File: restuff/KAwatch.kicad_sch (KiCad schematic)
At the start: 24 parts, among them J1 Conn_01x08, J2 USB_C_Receptacle_PowerOnly_6P, J3 Conn_01x02, J4 Conn_01x02, Q1 Q_NPN_BCE, SW1 SW_Push, U1 ESP32-WROOM-32E, U2 MCP73831-2-OT, U3 AMS1117-3.3

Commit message: footprint assignment complete
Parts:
- C1, C2, C3, C4, C5: footprint (none) -> Capacitor_SMD:C_0603_1608Metric
- D2: footprint (none) -> Diode_SMD:D_SOD-123
- J1: footprint RF_Module:ESP32-WROOM-32E -> Connector_PinHeader_2.54mm:PinHeader_1x08_P2.54mm_Vertical
- J3: footprint (none) -> Connector_JST:JST_PH_S2B-PH-K_1x02_P2.00mm_Horizontal
- Q1: footprint (none) -> Package_TO_SOT_SMD:SOT-23
- R1, R2, R3, R4, R5, R6, R7, R8: footprint (none) -> Resistor_SMD:R_0603_1608Metric
- SW1: footprint (none) -> Button_Switch_SMD:SW_SPST_TL3342
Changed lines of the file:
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@@
 			)
 		)
-		(property "Footprint" ""
+		(property "Footprint" "Resistor_SMD:R_0603_1608Metric"
 			(at 42.672 124.46 90)
 			(hide yes)
@@
 			)
 		)
-		(property "Footprint" ""
+		(property "Footprint" "Resistor_SMD:R_0603_1608Metric"
 			(at 116.332 104.14 90)
 			(hide yes)
@@
 			)
 		)
-		(property "Footprint" ""
+		(property "Footprint" "Capacitor_SMD:C_0603_1608Metric"
 			(at 60.6552 58.42 0)
 			(hide yes)
@@
 			)
 		)
-		(property "Footprint" ""
+		(property "Footprint" "Capacitor_SMD:C_0603_1608Metric"
 			(at 243.5352 77.47 0)
 			(hide yes)
@@
 			)
 		)
-		(property "Footprint" ""
+		(property "Footprint" "Button_Switch_SMD:SW_SPST_TL3342"
 			(at 113.03 81.28 0)
 			(hide yes)
@@
 			)
 		)
-		(property "Footprint" ""
+		(property "Footprint" "Resistor_SMD:R_0603_1608Metric"
 			(at 42.672 111.76 90)
 			(hide yes)
@@
 			)
 		)
-		(property "Footprint" "RF_Module:ESP32-WROOM-32E"
+		(property "Footprint" "Connector_PinHeader_2.54mm:PinHeader_1x08_P2.54mm_Vertical"
 			(at 118.11 128.27 0)
 			(hide yes)
@@
 			)
 		)
-		(property "Footprint" ""
+		(property "Footprint" "Resistor_SMD:R_0603_1608Metric"
 			(at 200.152 97.79 90)
 			(hide yes)
@@
 			)
 		)
-		(property "Footprint" ""
+		(property "Footprint" "Resistor_SMD:R_0603_1608Metric"
 			(at 220.472 105.41 90)
 			(hide yes)
@@
 			)
 		)
-		(property "Footprint" ""
+		(property "Footprint" "Diode_SMD:D_SOD-123"
 			(at 130.81 88.9 90)
 			(hide yes)
@@
 			)
 		)
-		(property "Footprint" ""
+		(property "Footprint" "Package_TO_SOT_SMD:SOT-23"
 			(at 138.43 107.95 0)
 			(hide yes)
@@
 			)
 		)
-		(property "Footprint" ""
+		(property "Footprint" "Capacitor_SMD:C_0603_1608Metric"
 			(at 252.4252 138.43 0)
 			(hide yes)
@@
 			)
 		)
-		(property "Footprint" ""
+		(property "Footprint" "Resistor_SMD:R_0603_1608Metric"
 			(at 210.312 97.79 90)
 			(hide yes)
@@
 			)
 		)
-		(property "Footprint" ""
+		(property "Footprint" "Connector_JST:JST_PH_S2B-PH-K_1x02_P2.00mm_Horizontal"
 			(at 257.81 113.03 0)
 			(hide yes)
@@
 			)
 		)
-		(property "Footprint" ""
+		(property "Footprint" "Capacitor_SMD:C_0603_1608Metric"
 			(at 223.2152 139.7 0)
 			(hide yes)
@@
 			)
 		)
-		(property "Footprint" ""
+		(property "Footprint" "Capacitor_SMD:C_0603_1608Metric"
 			(at 258.7752 104.14 0)
 			(hide yes)
@@
 			)
 		)
-		(property "Footprint" ""
+		(property "Footprint" "Resistor_SMD:R_0603_1608Metric"
 			(at 85.852 54.61 90)
 			(hide yes)
@@
 			)
 		)
-		(property "Footprint" ""
+		(property "Footprint" "Resistor_SMD:R_0603_1608Metric"
 			(at 46.482 54.61 90)
 			(hide yes)

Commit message: pcb editor phase 1
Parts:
- J2: footprint Package_TO_SOT_SMD:SOT-23-5 -> Connector_USB:USB_C_Receptacle_GCT_USB4125-xx-x_6P_TopMnt_Horizontal
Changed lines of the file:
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@@
 			)
 		)
-		(property "Footprint" "Package_TO_SOT_SMD:SOT-23-5"
+		(property "Footprint" "Connector_USB:USB_C_Receptacle_GCT_USB4125-xx-x_6P_TopMnt_Horizontal"
 			(at 189.23 82.55 0)
 			(hide yes)

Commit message: footprint assignment updated
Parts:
- J4: footprint LED_SMD:LED_WS2812B_PLCC4_5.0x5.0mm_P3.2mm -> Connector_PinHeader_2.54mm:PinHeader_1x02_P2.54mm_Vertical
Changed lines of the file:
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@@
 			)
 		)
-		(property "Footprint" "LED_SMD:LED_WS2812B_PLCC4_5.0x5.0mm_P3.2mm"
+		(property "Footprint" "Connector_PinHeader_2.54mm:PinHeader_1x02_P2.54mm_Vertical"
 			(at 140.97 88.9 0)
 			(hide yes)

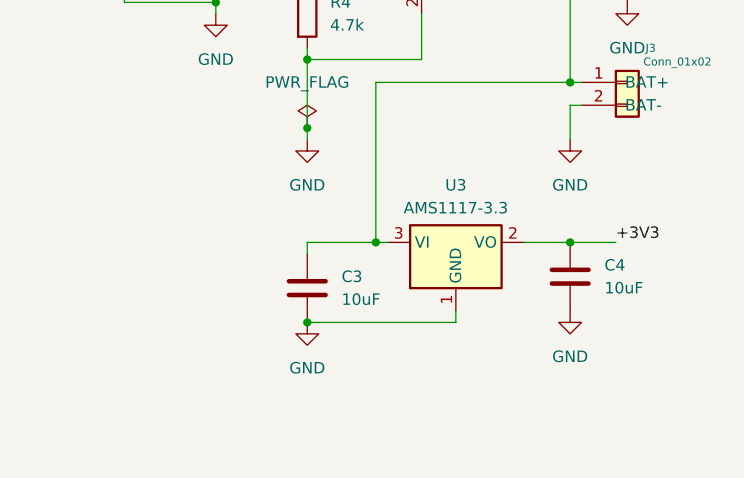
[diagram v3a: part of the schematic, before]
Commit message: voltage regulator changed to xc6620
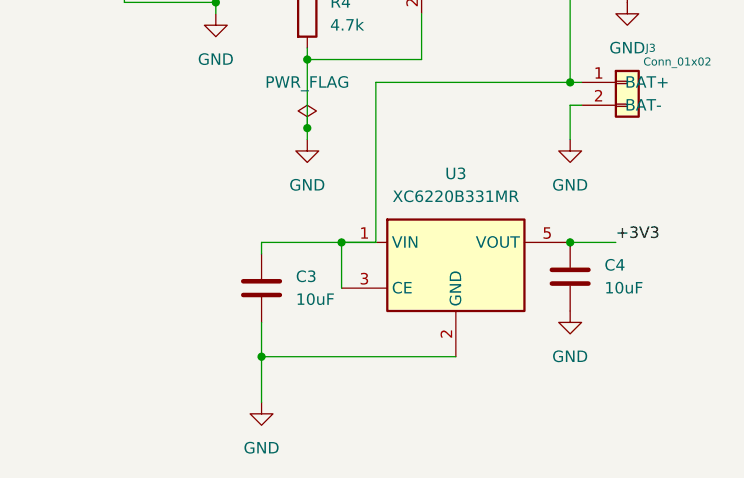
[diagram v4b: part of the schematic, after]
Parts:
- removed U3: AMS1117-3.3, Package_TO_SOT_SMD:SOT-223-3_TabPin2, symbol Regulator_Linear:AMS1117-3.3
- added U3: XC6220B331MR, Package_TO_SOT_SMD:SOT-23-5, symbol Regulator_Linear:XC6220B331MR
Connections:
- net +3V3: now also U3.5 (VOUT)
- net GND: now also U3.2 (GND)
- net at C2.1, C3.1, J3.1 (BAT+)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: now also U3.1 (VIN), U3.3 (CE)
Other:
- moved on the sheet: C3
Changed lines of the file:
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@@
 	(paper "A4")
 	(junction
+		(at 226.06 130.81)
+		(diameter 0)
+		(color 0 0 0 0)
+	)
+	(junction
 		(at 135.89 95.25)
 		(diameter 0)
@@
 	)
 	(junction
-		(at 229.87 130.81)
+		(at 217.17 143.51)
 		(diameter 0)
 		(color 0 0 0 0)
@@
 	)
 	(junction
-		(at 222.25 139.7)
-		(diameter 0)
-		(color 0 0 0 0)
-	)
-	(junction
 		(at 251.46 95.25)
 		(diameter 0)
@@
 	(wire
 		(pts
-			(xy 222.25 139.7) (xy 238.76 139.7)
-		)
-		(stroke
-			(width 0)
-			(type default)
-		)
-	)
-	(wire
-		(pts
 			(xy 85.09 88.9) (xy 110.49 88.9)
 		)
@@
 	(wire
 		(pts
-			(xy 222.25 130.81) (xy 229.87 130.81)
+			(xy 217.17 130.81) (xy 229.87 130.81)
 		)
 		(stroke
@@
 	(wire
 		(pts
-			(xy 246.38 130.81) (xy 251.46 130.81)
+			(xy 85.09 114.3) (xy 87.63 114.3)
 		)
 		(stroke
@@
 	(wire
 		(pts
-			(xy 85.09 114.3) (xy 87.63 114.3)
+			(xy 251.46 95.25) (xy 251.46 113.03)
 		)
 		(stroke
@@
 	(wire
 		(pts
-			(xy 251.46 95.25) (xy 251.46 113.03)
+			(xy 226.06 130.81) (xy 226.06 135.89)
 		)
 		(stroke
@@
 	(wire
 		(pts
+			(xy 217.17 148.59) (xy 217.17 143.51)
+		)
+		(stroke
+			(width 0)
+			(type default)
+		)
+	)
+	(wire
+		(pts
 			(xy 245.11 95.25) (xy 251.46 95.25)
 		)
@@
 	(wire
 		(pts
-			(xy 238.76 138.43) (xy 238.76 139.7)
-		)
-		(stroke
-			(width 0)
-			(type default)
-		)
-	)
-	(wire
-		(pts
 			(xy 85.09 78.74) (xy 109.22 78.74)
 		)
@@
 	(wire
 		(pts
+			(xy 217.17 143.51) (xy 217.17 139.7)
+		)
+		(stroke
+			(width 0)
+			(type default)
+		)
+	)
+	(wire
+		(pts
 			(xy 130.81 95.25) (xy 135.89 95.25)
 		)
@@
 	(wire
 		(pts
-			(xy 229.87 130.81) (xy 231.14 130.81)
-		)
-		(stroke
-			(width 0)
-			(type default)
-		)
-	)
-	(wire
-		(pts
 			(xy 242.57 59.69) (xy 242.57 69.85)
 		)
@@
 	(wire
 		(pts
-			(xy 222.25 130.81) (xy 222.25 132.08)
+			(xy 217.17 130.81) (xy 217.17 132.08)
 		)
 		(stroke
@@
 	(wire
 		(pts
+			(xy 217.17 143.51) (xy 238.76 143.51)
+		)
+		(stroke
+			(width 0)
+			(type default)
+		)
+	)
+	(wire
+		(pts
 			(xy 110.49 125.73) (xy 113.03 125.73)
 		)
@@
 	)
 	(symbol
+		(lib_id "Regulator_Linear:XC6220B331MR")
+		(at 238.76 133.35 0)
+		(unit 1)
+		(body_style 1)
+		(exclude_from_sim no)
+		(in_bom yes)
+		(on_board yes)
+		(in_pos_files yes)
+		(dnp no)
+		(fields_autoplaced yes)
+		(property "Reference" "U3"
+			(at 238.76 123.19 0)
+			(show_name no)
+			(do_not_autoplace no)
+			(effects
+				(font
+					(size 1.27 1.27)
+				)
+			)
+		)
+		(property "Value" "XC6220B331MR"
+			(at 238.76 125.73 0)
+			(show_name no)
+			(do_not_autoplace no)
+			(effects
+				(font
+					(size 1.27 1.27)
+				)
+			)
+		)
+		(property "Footprint" "Package_TO_SOT_SMD:SOT-23-5"
+			(at 238.76 133.35 0)
+			(hide yes)
+			(show_name no)
+			(do_not_autoplace no)
+			(effects
+				(font
+					(size 1.27 1.27)
+				)
+			)
+		)
+		(property "Datasheet" "https://www.torexsemi.com/file/xc6220/XC6220.pdf"
+			(at 257.81 158.75 0)
+			(hide yes)
+			(show_name no)
+			(do_not_autoplace no)
+			(effects
+				(font
+					(size 1.27 1.27)
+				)
+			)
+		)
+		(property "Description" "1A, Low Drop-out Voltage Regulator, Fixed Output 3.3V, SOT-23-5"
+			(at 238.76 133.35 0)
+			(hide yes)
+			(show_name no)
+			(do_not_autoplace no)
+			(effects
+				(font
+					(size 1.27 1.27)
+				)
+			)
+		)
+		(pin "5"
+		)
+		(pin "4"
+		)
+		(pin "3"
+		)
+		(pin "1"
+		)
+		(pin "2"
+		)
+		(instances
+			(project "KAwatch"
+				(path "/d13b4dc6-0a30-4e9b-a54d-0e2e2d77415c"
+					(reference "U3")
+					(unit 1)
+				)
+			)
+		)
+	)
+	(symbol
 		(lib_id "Device:C")
 		(at 59.69 54.61 0)
@@
 	(symbol
 		(lib_id "power:GND")
-		(at 222.25 139.7 0)
+		(at 217.17 148.59 0)
 		(unit 1)
 		(body_style 1)
@@
 		(fields_autoplaced yes)
 		(property "Reference" "#PWR08"
-			(at 222.25 146.05 0)
+			(at 217.17 154.94 0)
 			(hide yes)
 			(show_name no)
@@
 		)
 		(property "Value" "GND"
-			(at 222.25 144.78 0)
+			(at 217.17 153.67 0)
 			(show_name no)
 			(do_not_autoplace no)
@@
 		)
 		(property "Footprint" ""
-			(at 222.25 139.7 0)
+			(at 217.17 148.59 0)
 			(hide yes)
 			(show_name no)
@@
 		)
 		(property "Datasheet" ""
-			(at 222.25 139.7 0)
+			(at 217.17 148.59 0)
 			(hide yes)
 			(show_name no)
@@
 		)
 		(property "Description" "Power symbol creates a global label with name \"GND\" , ground"
-			(at 222.25 139.7 0)
+			(at 217.17 148.59 0)
 			(hide yes)
 			(show_name no)
@@
 	(symbol
 		(lib_id "Device:C")
-		(at 222.25 135.89 0)
+		(at 217.17 135.89 0)
 		(unit 1)
 		(body_style 1)
@@
 		(fields_autoplaced yes)
 		(property "Reference" "C3"
-			(at 226.06 134.6199 0)
+			(at 220.98 134.6199 0)
 			(show_name no)
 			(do_not_autoplace no)
@@
 		)
 		(property "Value" "10uF"
-			(at 226.06 137.1599 0)
+			(at 220.98 137.1599 0)
 			(show_name no)
 			(do_not_autoplace no)
@@
 		)
 		(property "Footprint" "Capacitor_SMD:C_0603_1608Metric"
-			(at 223.2152 139.7 0)
+			(at 218.1352 139.7 0)
 			(hide yes)
 			(show_name no)
@@
 		)
 		(property "Datasheet" ""
-			(at 222.25 135.89 0)
+			(at 217.17 135.89 0)
 			(hide yes)
 			(show_name no)
@@
 		)
 		(property "Description" "Unpolarized capacitor"
-			(at 222.25 135.89 0)
+			(at 217.17 135.89 0)
 			(hide yes)
 			(show_name no)
@@
 					(unit 1)
 				)
-			)
-		)
-	)
-	(symbol
-		(lib_id "Regulator_Linear:AMS1117-3.3")
-		(at 238.76 130.81 0)
-		(unit 1)
-		(body_style 1)
-		(exclude_from_sim no)
-		(in_bom yes)
-		(on_board yes)
-		(in_pos_files yes)
-		(dnp no)
-		(fields_autoplaced yes)
-		(property "Reference" "U3"
-			(at 238.76 124.46 0)
-			(show_name no)
-			(do_not_autoplace no)
-			(effects
-				(font
-					(size 1.27 1.27)
-				)
-			)
-		)
-		(property "Value" "AMS1117-3.3"
-			(at 238.76 127 0)
-			(show_name no)
-			(do_not_autoplace no)
-			(effects
-				(font
-					(size 1.27 1.27)
-				)
-			)
-		)
-		(property "Footprint" "Package_TO_SOT_SMD:SOT-223-3_TabPin2"
-			(at 238.76 125.73 0)
-			(hide yes)
-			(show_name no)
-			(do_not_autoplace no)
-			(effects
-				(font
-					(size 1.27 1.27)
-				)
-			)
-		)
-		(property "Datasheet" "http://www.advanced-monolithic.com/pdf/ds1117.pdf"
-			(at 241.3 137.16 0)
-			(hide yes)
-			(show_name no)
-			(do_not_autoplace no)
-			(effects
-				(font
-					(size 1.27 1.27)
-				)
-			)
-		)
-		(property "Description" "1A Low Dropout regulator, positive, 3.3V fixed output, SOT-223"
-			(at 238.76 130.81 0)
-			(hide yes)
-			(show_name no)
-			(do_not_autoplace no)
-			(effects
-				(font
-					(size 1.27 1.27)
-				)
-			)
-		)
-		(pin "3"
-		)
-		(pin "2"
-		)
-		(pin "1"
-		)
-		(instances
-			(project "KAwatch"
-				(path "/d13b4dc6-0a30-4e9b-a54d-0e2e2d77415c"
-					(reference "U3")
-					(unit 1)
-				)

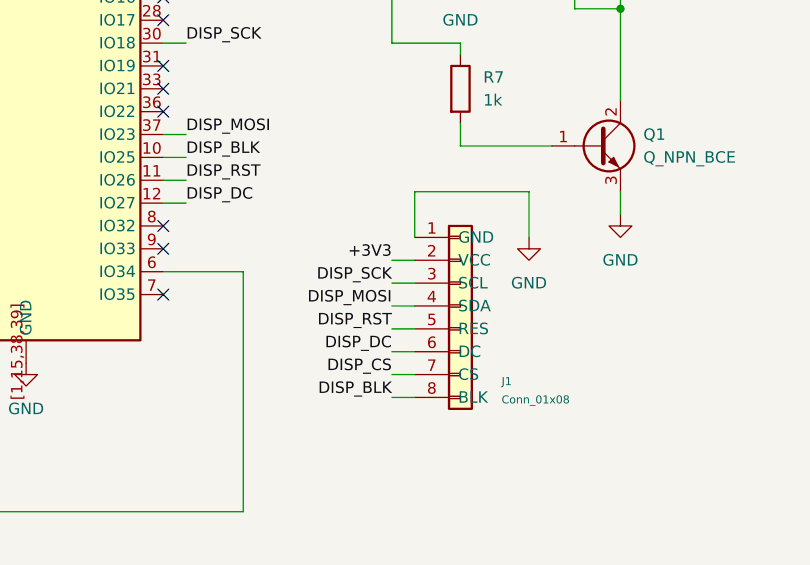
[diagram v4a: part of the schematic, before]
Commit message: display connector pins updated
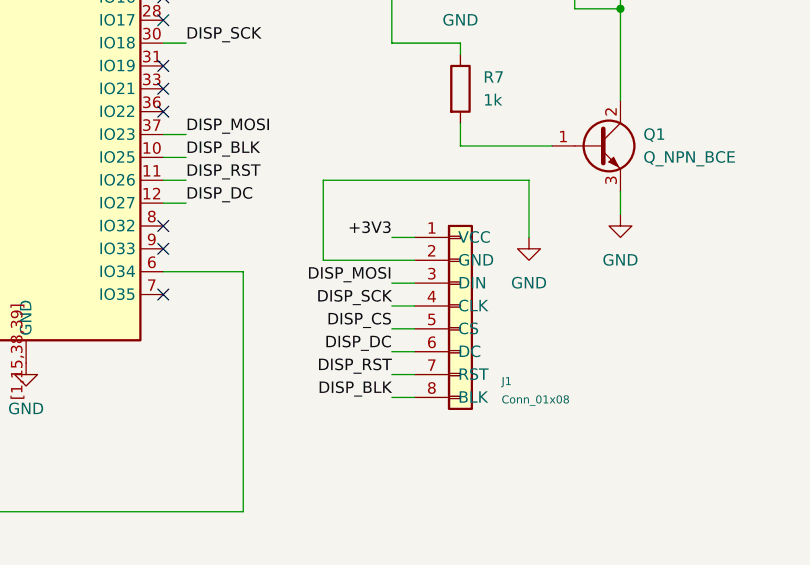
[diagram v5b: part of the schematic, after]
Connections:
- net +3V3: now also J1.1 (VCC); no longer J1.2 (VCC)
- net DISP_CS: now also J1.5 (CS); no longer J1.7 (CS)
- net DISP_MOSI: now also J1.3 (DIN); no longer J1.4 (SDA)
- net DISP_RST: now also J1.7 (RST); no longer J1.5 (RES)
- net GND: now also J1.2 (GND); no longer J1.1 (GND)
- net DISP_SCK: now reaches U1.30 (IO18)
- net DISP_SCK: now also J1.4 (CLK); no longer J1.3 (SCL)
